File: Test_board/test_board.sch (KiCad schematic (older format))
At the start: 35 parts, among them J1 CONN_01X03_MALE, J11 CONN_01X03_MALE, J12 CONN_01X05, J15 CONN_01X05, J2 CONN_02X20, J3 CONN_01X06, J4 CONN_02X20, J5 USB_A, J6 USB_A, J7 USB_A, J8 DB9_FEMALE, Q1 2N7002, Q2 2N7002, U1 MAX16056, U2 PIC24HJ128GP502-I/MM, U4 STM32F302K8U6

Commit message: Deleted PCB files, removed MCUs and 1 USB port from schematic, cleaned up schematic
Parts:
- removed C1, C19, C2, C20, C21: 0.1uF, Capacitors_SMD:C_0805, symbol C
- removed C3: 10uF, Capacitors_SMD:C_0805, symbol C
- removed J11: CONN_01X03_MALE, Pin_Headers:Pin_Header_Straight_1x03_Pitch2.54mm, symbol CONN_01X03_MALE
- removed J12, J15: CONN_01X05, Pin_Headers:Pin_Header_Straight_1x05_Pitch2.54mm, symbol CONN_01X05
- removed J6: USB_A, aleksandr_footprints:USB_A_Board, symbol USB_A-RESCUE-test_board
- removed Q1, Q2: 2N7002, TO_SOT_Packages_SMD:SOT-23, symbol Q_PMOS_GSD
- removed R18, R19, R2, R20, R3, R4: 4k7, Resistors_SMD:R_0805, symbol R
- removed U2: PIC24HJ128GP502-I/MM, Housings_DFN_QFN:QFN-28-1EP_6x6mm_Pitch0.65mm, symbol PIC24HJ128GP502-I/MM
- removed U4: STM32F302K8U6, Housings_DFN_QFN:QFN-32-1EP_5x5mm_Pitch0.5mm, symbol STM32F302K8U6
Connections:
- net labels removed: JTCK, JTDI, JTDO, JTMS, JTRST, M4_BOOT, ProgC, ProgD, USBB_D+, USBB_D-, ~MCU_Reset
- wire segments 166 -> 100
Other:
- note added: "x2 USB A (Arietta G25 as host)\n"
- note removed: "Arm Cortex M4 - \nTest MCU 2"
- note removed: "Keep jumper in grounded\nposition unless needed \notherwise"
- note removed: "PIC24 - Test MCU 1"
- note removed: "x3 USB A (Arietta G25 as host)\n"
- moved on the sheet: C4, C5, C6, J1, R1, R5, R6, U1

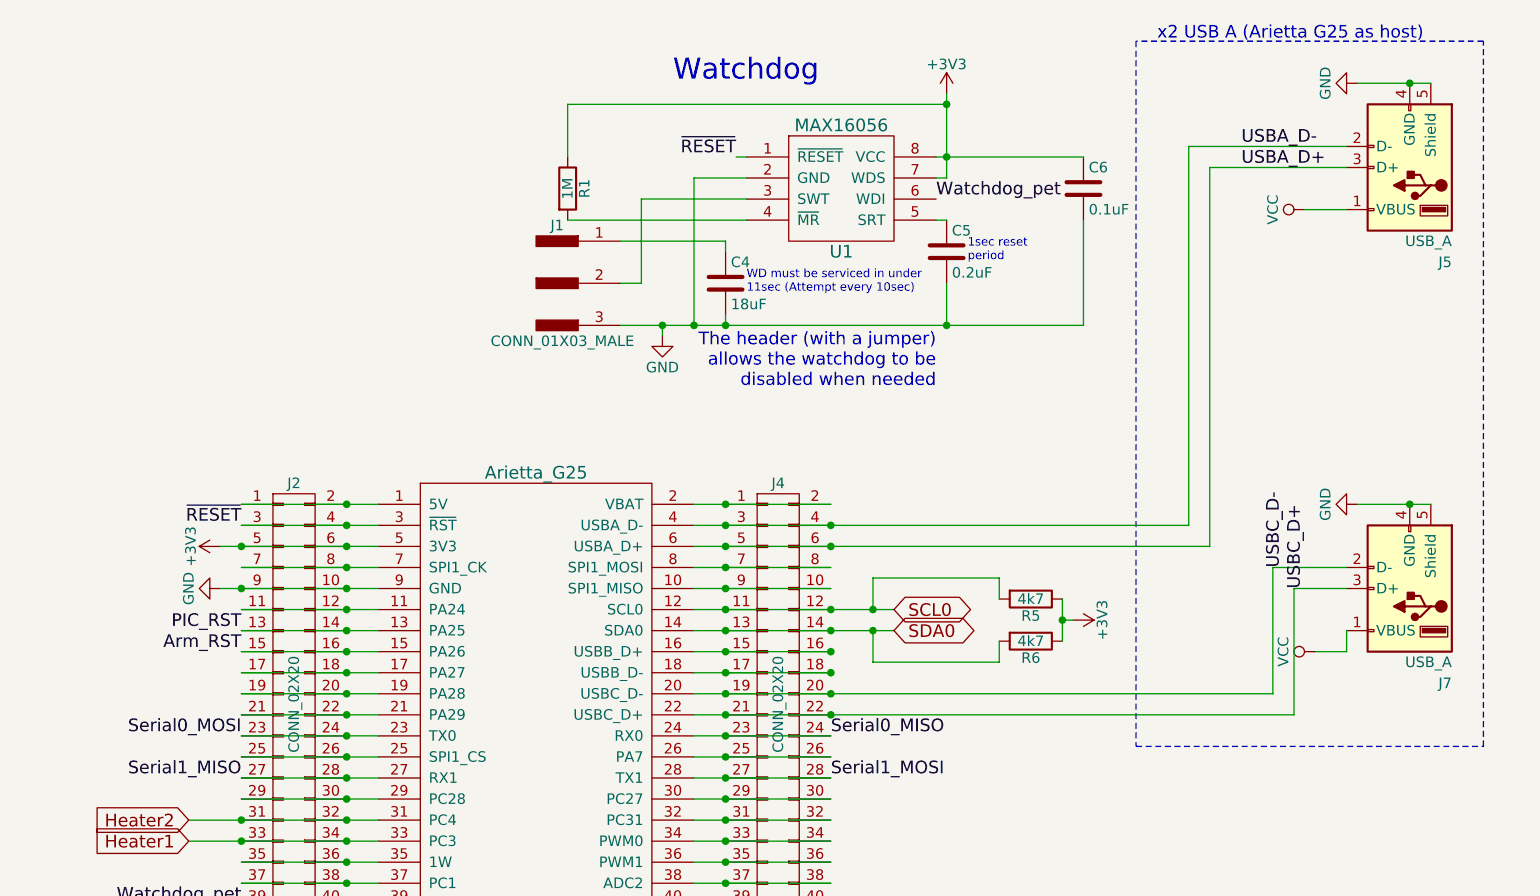
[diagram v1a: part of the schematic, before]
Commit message: Started defining STM32F303RE component
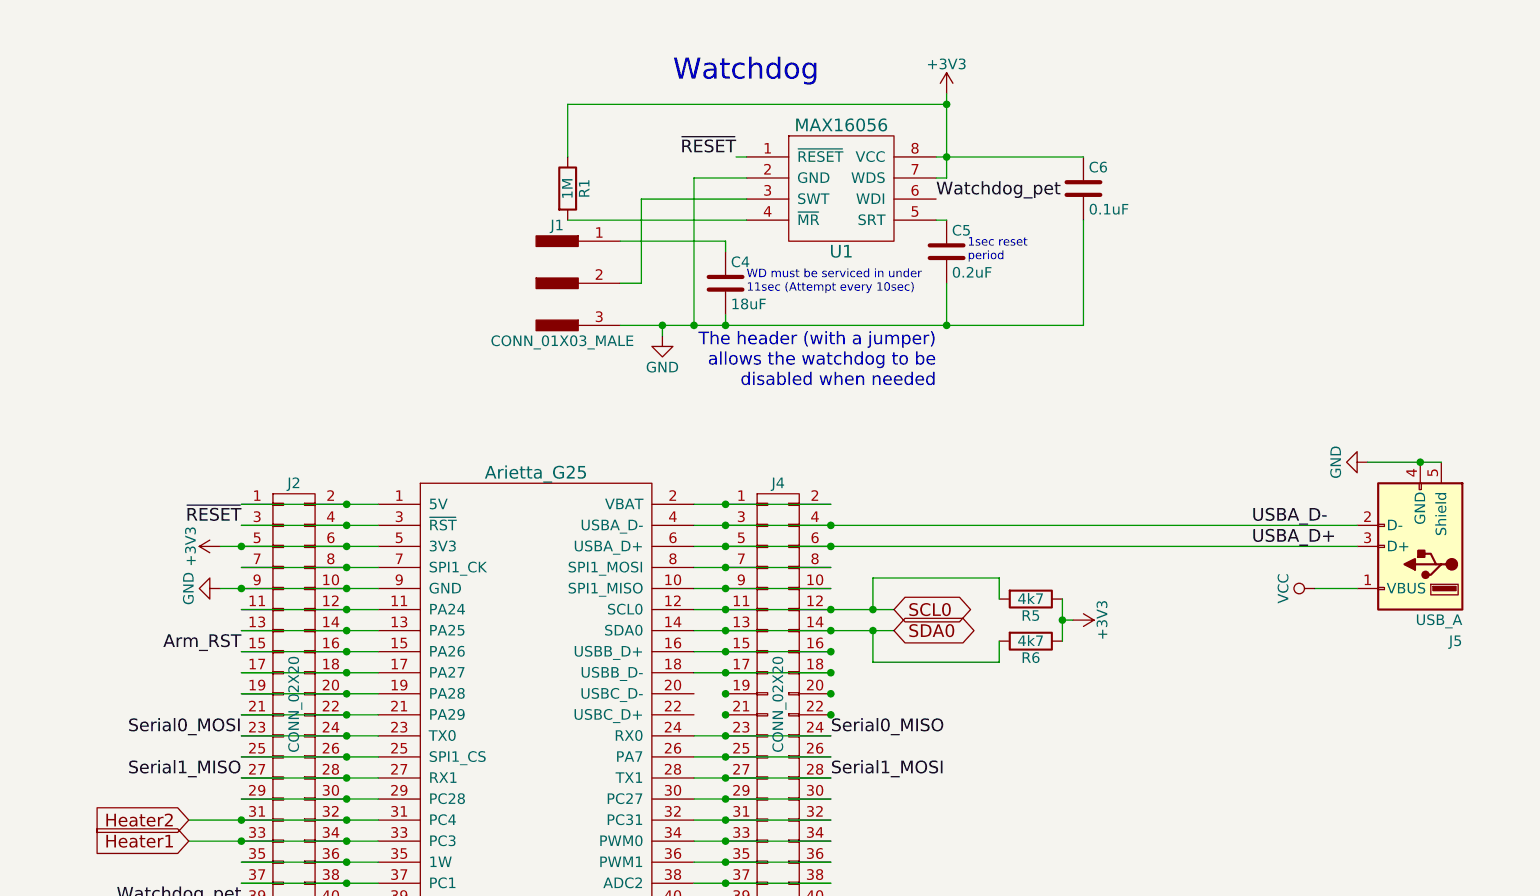
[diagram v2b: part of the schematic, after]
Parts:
- removed J7: USB_A, aleksandr_footprints:USB_A_Board, symbol USB_A-RESCUE-test_board
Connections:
- net PIC_RST: no longer names the net of J2.13 (P13), J2.14 (P14), OBC1.13 (PA25)
- removed net USBC_D+: J4.21 (P21), J4.22 (P22), OBC1.22 (USBC_D+)
- removed net USBC_D-: J4.19 (P19), J4.20 (P20), OBC1.20 (USBC_D-)
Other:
- note removed: "x2 USB A (Arietta G25 as host)\n"
- moved on the sheet: J5
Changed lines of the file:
@@
 L USB_A-RESCUE-test_board J5
 U 1 1 5995E3C3
-P 10300 1200
-F 0 "J5" H 10100 1650 50  0000 L CNN
-F 1 "USB_A" H 10100 1550 50  0000 L CNN
-F 2 "aleksandr_footprints:USB_A_Board" H 10450 1150 50  0001 C CNN
-F 3 "" H 10450 1150 50  0001 C CNN
-	1    10300 1200
-	-1   0    0    1
-$EndComp
-$Comp
-L USB_A-RESCUE-test_board J7
-U 1 1 5995E4B2
-P 10300 3200
-F 0 "J7" H 10100 3650 50  0000 L CNN
-F 1 "USB_A" H 10100 3550 50  0000 L CNN
-F 2 "aleksandr_footprints:USB_A_Board" H 10450 3150 50  0001 C CNN
-F 3 "" H 10450 3150 50  0001 C CNN
-	1    10300 3200
+P 10350 3000
+F 0 "J5" H 10150 3450 50  0000 L CNN
+F 1 "USB_A" H 10150 3350 50  0000 L CNN
+F 2 "aleksandr_footprints:USB_A_Board" H 10500 2950 50  0001 C CNN
+F 3 "" H 10500 2950 50  0001 C CNN
+	1    10350 3000
 	-1   0    0    1
 $EndComp
@@
 L GND #PWR05
 U 1 1 5995FB3E
-P 10050 800
-F 0 "#PWR05" H 10050 550 50  0001 C CNN
-F 1 "GND" H 10050 650 50  0000 C CNN
-F 2 "" H 10050 800 50  0001 C CNN
-F 3 "" H 10050 800 50  0001 C CNN
-	1    10050 800
-	0    1    1    0
-$EndComp
-$Comp
-L GND #PWR07
-U 1 1 5995FB7C
-P 10050 2800
-F 0 "#PWR07" H 10050 2550 50  0001 C CNN
-F 1 "GND" H 10050 2650 50  0000 C CNN
-F 2 "" H 10050 2800 50  0001 C CNN
-F 3 "" H 10050 2800 50  0001 C CNN
-	1    10050 2800
+P 10100 2600
+F 0 "#PWR05" H 10100 2350 50  0001 C CNN
+F 1 "GND" H 10100 2450 50  0000 C CNN
+F 2 "" H 10100 2600 50  0001 C CNN
+F 3 "" H 10100 2600 50  0001 C CNN
+	1    10100 2600
 	0    1    1    0
 $EndComp
@@
 Text Label 7550 3900 0    60   ~ 0
 Serial0_MISO
-Text Label 4750 3400 2    60   ~ 0
-PIC_RST
 $Comp
 L MAX16056 U1
@@
 Connection ~ 7050 2800
 Wire Wire Line
-	6900 2900 9250 2900
+	6900 2900 10050 2900
 Connection ~ 7050 2900
 Wire Wire Line
-	6900 3000 9350 3000
+	6900 3000 10050 3000
 Connection ~ 7050 3000
 Wire Wire Line
@@
 Connection ~ 7050 3500
 Connection ~ 7050 3600
-Wire Wire Line
-	6900 3700 9650 3700
 Connection ~ 7050 3700
-Wire Wire Line
-	6900 3800 9750 3800
 Connection ~ 7050 3800
 Wire Wire Line
@@
 Connection ~ 7550 3300
 Connection ~ 7550 3400
-Wire Wire Line
-	9250 2900 9250 1100
-Wire Wire Line
-	9250 1100 10000 1100
 Connection ~ 7550 2900
-Wire Wire Line
-	10000 1200 9350 1200
-Wire Wire Line
-	9350 1200 9350 3000
 Connection ~ 7550 3000
 Connection ~ 7550 3500
 Connection ~ 7550 3600
-Wire Wire Line
-	9650 3700 9650 3100
-Wire Wire Line
-	9650 3100 10000 3100
 Connection ~ 7550 3700
-Wire Wire Line
-	9750 3800 9750 3200
-Wire Wire Line
-	9750 3200 10000 3200
 Connection ~ 7550 3800
 Wire Wire Line
-	10050 800  10400 800
-Wire Wire Line
-	10050 2800 10400 2800
-Wire Wire Line
-	10000 3500 10000 3400
-Wire Wire Line
-	9850 3500 10000 3500
-Wire Wire Line
-	9800 1400 10000 1400
+	10100 2600 10450 2600
+Wire Wire Line
+	9850 3200 10050 3200
 Wire Wire Line
 	6100 7500 6100 7400
 Wire Wire Line
 	6500 7500 6500 7400
-Connection ~ 10300 800
-Connection ~ 10300 2800
+Connection ~ 10350 2600
 Wire Wire Line
 	10000 5100 7000 5100
@@
 Text Notes 7700 5450 0    60   ~ 0
 Serial comms with standard DB9 connector\n
-Wire Notes Line
-	9000 600  9000 3950
-Wire Notes Line
-	9000 3950 10650 3950
-Wire Notes Line
-	10650 3950 10650 600
-Wire Notes Line
-	10650 600  9000 600
-Text Notes 9100 600  0    60   ~ 0
-x2 USB A (Arietta G25 as host)\n
 Text GLabel 4500 4400 0    60   Input ~ 0
 Heater1
@@
 Connection ~ 4750 4300
 Connection ~ 4750 4400
-Text Label 9500 1100 0    60   ~ 0
+Text Label 9550 2900 0    60   ~ 0
 USBA_D-
-Text Label 9500 1200 0    60   ~ 0
+Text Label 9550 3000 0    60   ~ 0
 USBA_D+
-Text Label 9700 3100 1    60   ~ 0
-USBC_D-
-Text Label 9800 3200 1    60   ~ 0
-USBC_D+
 Text Label 7250 5100 0    60   ~ 0
 DB_TX
@@
 L VCC #PWR?
 U 1 1 59B5D45E
-P 9800 1400
-F 0 "#PWR?" H 9800 1250 50  0001 C CNN
-F 1 "VCC" H 9800 1550 50  0000 C CNN
-F 2 "" H 9800 1400 50  0001 C CNN
-F 3 "" H 9800 1400 50  0001 C CNN
-	1    9800 1400
+P 9850 3200
+F 0 "#PWR?" H 9850 3050 50  0001 C CNN
+F 1 "VCC" H 9850 3350 50  0000 C CNN
+F 2 "" H 9850 3200 50  0001 C CNN
+F 3 "" H 9850 3200 50  0001 C CNN
+	1    9850 3200
 	0    -1   -1   0
 $EndComp
-$Comp
-L VCC #PWR?
-U 1 1 59B5D50C
-P 9850 3500
-F 0 "#PWR?" H 9850 3350 50  0001 C CNN
-F 1 "VCC" H 9850 3650 50  0000 C CNN
-F 2 "" H 9850 3500 50  0001 C CNN
-F 3 "" H 9850 3500 50  0001 C CNN
-	1    9850 3500
-	0    -1   -1   0
-$EndComp

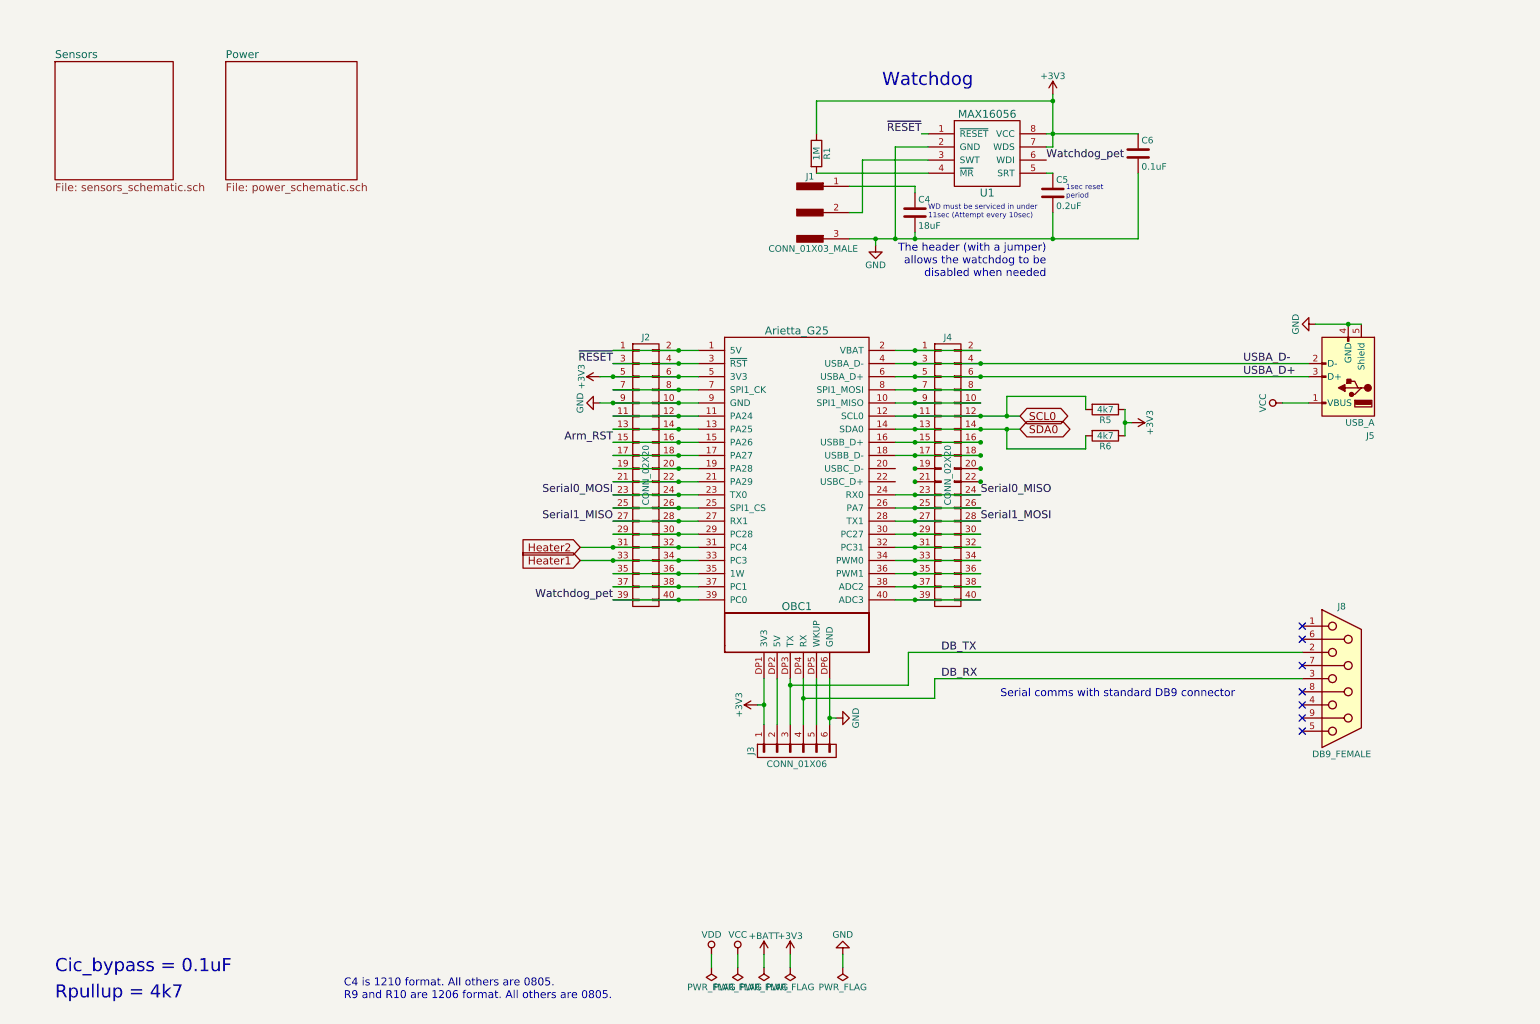
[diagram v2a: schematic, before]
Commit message: Updated schematic around MCU, defined comms pinout. Started setup of CAN bus connectors.
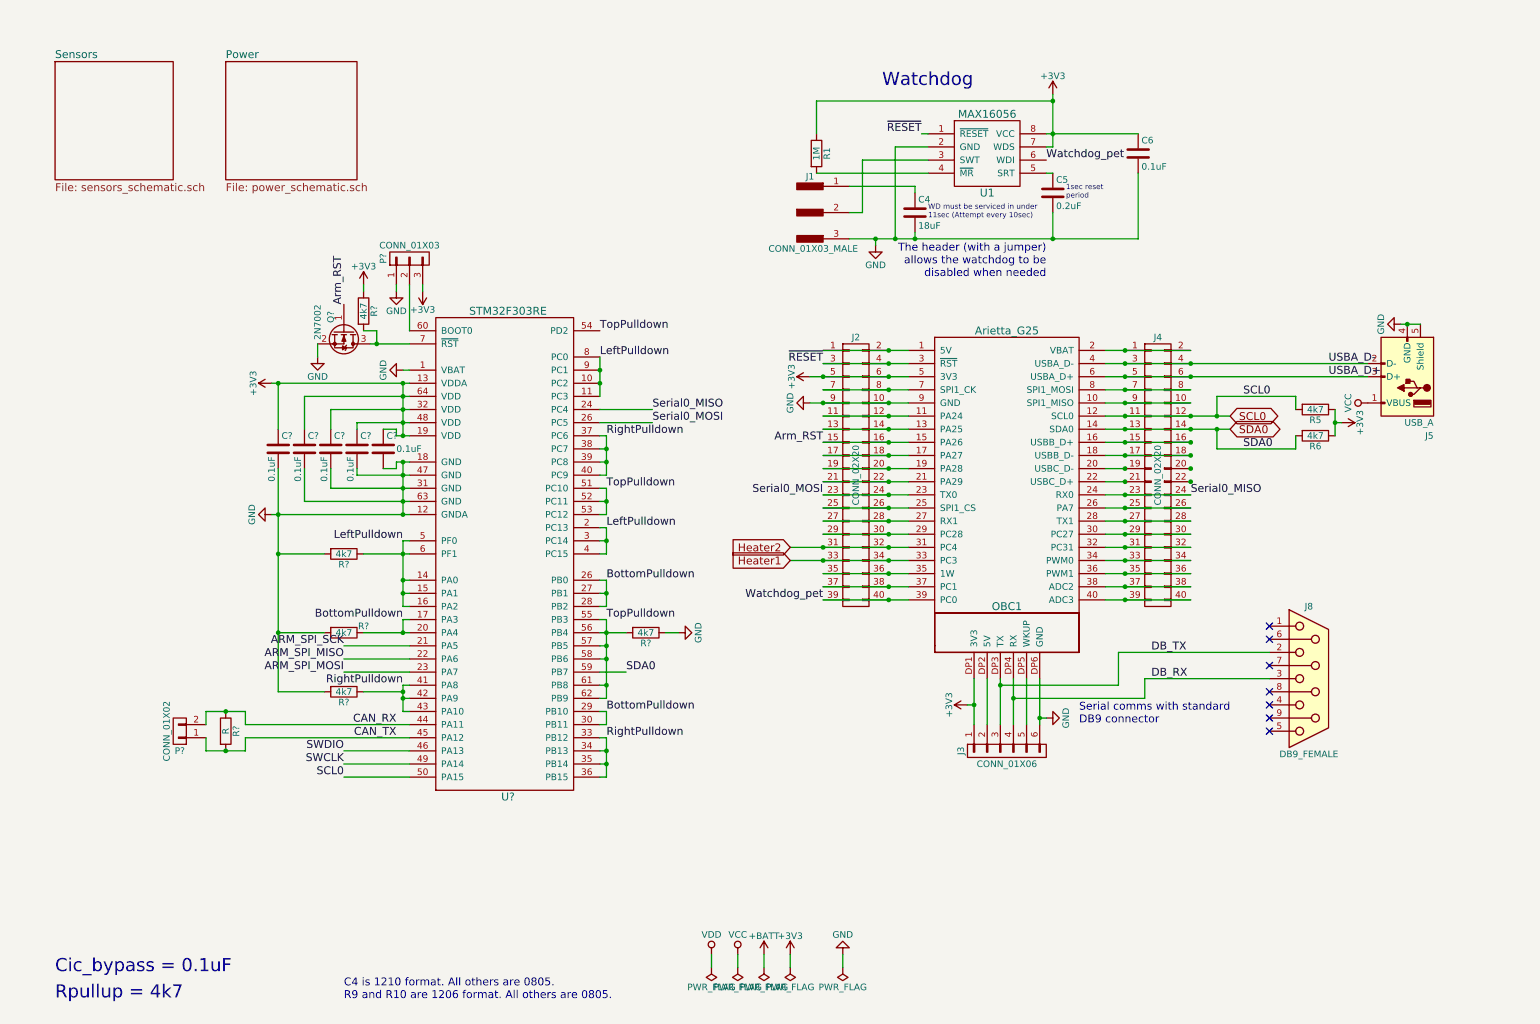
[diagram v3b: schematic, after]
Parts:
- added C? (x5): 0.1uF, symbol C
- added P?: CONN_01X03, symbol CONN_01X03
- added P?: CONN_01X02, symbol CONN_01X02
- added Q?: 2N7002, symbol Q_NMOS_GSD
- added R? (x5): 4k7, symbol R
- added R?: R, symbol R
- added U?: STM32F303RE, symbol STM32F303RE
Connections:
- net +3V3: now also C?.1, C?.1, C?.1, C?.1, C?.1, P?.3 (P3), R?.1, U?.13 (VDDA), U?.19 (VDD), U?.32 (VDD), U?.48 (VDD), U?.64 (VDD)
- net Arm_RST: now also Q?.1 (G)
- net GND: now also C?.2, C?.2, C?.2, C?.2, C?.2, P?.1 (P1), Q?.2 (S), R?.1, R?.2, R?.2, R?.2, U?.1 (VBAT), U?.12 (GNDA), U?.18 (GND), U?.31 (GND), U?.47 (GND), U?.63 (GND)
- net SCL0: now also U?.50 (PA15)
- net SDA0: now also U?.59 (PB7)
- net Serial0_MISO: now also U?.24 (PC4)
- net Serial0_MOSI: now also U?.26 (PC5)
- net at OBC1.20 (USBC_D-): now also J4.19 (P19)
- net at OBC1.22 (USBC_D+): now also J4.21 (P21)
- net Serial1_MISO: no longer names the net of J2.27 (P27), J2.28 (P28), OBC1.27 (RX1)
- net Serial1_MOSI: no longer names the net of J4.27 (P27), J4.28 (P28), OBC1.28 (TX1)
- new net: P?.2 (P2), U?.60 (BOOT0)
- new net: Q?.3 (D), R?.2, U?.7 (~RST)
- new net ARM_SPI_MISO: U?.22 (PA6)
- new net ARM_SPI_MOSI: U?.23 (PA7)
- new net ARM_SPI_SCK: U?.21 (PA5)
- new net BottomPulldown: R?.1, U?.17 (PA3), U?.20 (PA4), U?.26 (PC5), U?.27 (PB1), U?.28 (PB2), U?.29 (PB10), U?.30 (PB11)
- new net CAN_RX: P?.2 (P2), R?.1, U?.44 (PA11)
- new net CAN_TX: P?.1 (P1), R?.2, U?.45 (PA12)
- new net LeftPulldown: R?.1, U?.10 (PC2), U?.11 (PC3), U?.14 (PA0), U?.15 (PA1), U?.16 (PA2), U?.2 (PC13), U?.3 (PC14), U?.4 (PC15), U?.5 (PF0), U?.6 (PF1), U?.8 (PC0), U?.9 (PC1)
- new net RightPulldown: R?.1, U?.33 (PB12), U?.34 (PB13), U?.35 (PB14), U?.36 (PB15), U?.37 (PC6), U?.38 (PC7), U?.39 (PC8), U?.40 (PC9), U?.41 (PA8), U?.42 (PA9), U?.43 (PA10)
- new net SWCLK: U?.49 (PA14)
- new net SWDIO: U?.46 (PA13)
- new net TopPulldown: R?.2, U?.51 (PC10), U?.52 (PC11), U?.53 (PC12), U?.54 (PD2), U?.55 (PB3), U?.56 (PB4), U?.57 (PB5), U?.58 (PB6), U?.61 (PB8), U?.62 (PB9)
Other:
- note added: "Serial comms with standard \nDB9 connector\n"
- note removed: "Serial comms with standard DB9 connector\n"
- moved on the sheet: J2, J3, J4, J5, J8, OBC1, R5, R6
